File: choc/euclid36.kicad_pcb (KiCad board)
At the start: 2 copper layers, 248.2 x 127 mm, 112 parts, among them SW10 SW_PUSH, SW11 SW_PUSH, SW12 SW_PUSH, SW14 SW_PUSH, SW15 SW_PUSH, SW16 SW_PUSH, SW17 SW_PUSH, SW18 SW_PUSH, SW19 SW_PUSH, SW2 SW_PUSH, SW20 SW_PUSH, SW21 SW_PUSH, SW22 SW_PUSH, SW23 SW_PUSH, SW25 SW_PUSH, SW26 SW_PUSH, SW27 SW_PUSH, SW28 SW_PUSH, SW29 SW_PUSH, SW3 SW_PUSH, SW31 SW_PUSH, SW32 SW_PUSH, SW33 SW_PUSH, SW34 SW_PUSH, SW35 SW_PUSH, SW37 SW_PUSH, SW38 SW_PUSH, SW39 SW_PUSH, SW4 SW_PUSH, SW40 SW_PUSH, SW41 SW_PUSH, SW42 SW_PUSH, SW5 SW_PUSH, SW6 SW_PUSH, SW8 SW_PUSH, SW9 SW_PUSH, U2 ATmega32U4-MU, Y1 XTAL

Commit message: Wired everything. Not too happy with it, but I think it works
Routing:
- net VCC: track 0.00 -> 656.2 mm, vias 0 -> 30
- net col3: track 0.00 -> 541.0 mm, vias 0 -> 18
- net GND: track 164.3 -> 669.2 mm, vias 2 -> 12
- net col4: track 0.00 -> 501.9 mm, vias 0 -> 22
- net col2: track 0.00 -> 416.9 mm, vias 0 -> 17
- net col1: track 0.00 -> 387.6 mm, vias 0 -> 15
- net row6: track 0.00 -> 274.4 mm, vias 0 -> 6
- net col0: track 0.00 -> 231.2 mm, vias 0 -> 2
- net row5: track 0.00 -> 200.6 mm, vias 0 -> 4
- net col5: track 0.00 -> 193.8 mm, vias 0 -> 12
- net row3: track 0.00 -> 185.9 mm, vias 0 -> 10
- net row4: track 0.00 -> 169.3 mm, vias 0 -> 6
- net row2: track 0.00 -> 163.8 mm
- net row1: track 0.00 -> 137.2 mm
- net row0: track 9.49 -> 117.2 mm
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
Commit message: Small fixes
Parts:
- moved L6 1.40 mm to (47.3, 71.6)
- moved L11 1.17 mm to (252.7, 71.1)
- moved L5 0.85 mm to (64.0, 45.0)
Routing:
- net GND: track 669.2 -> 672.9 mm
- net Net-(L5-Pad2): track 69.8 -> 72.9 mm
- net Net-(L11-Pad2): track 27.8 -> 29.1 mm
- net Net-(L10-Pad2): track 45.2 -> 44.3 mm
- net VCC: track 656.2 -> 657.1 mm
- net Net-(L6-Pad2): track 80.9 -> 80.3 mm

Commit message: complete, ready for fabrication, though might change mini usb to micro usb before doing so
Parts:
- removed D1: PRTR5V0U2X, euclid36-libs:SOT-143B
- removed R3: 5.1k, Resistor_SMD:R_0805_2012Metric_Pad1.20x1.40mm_HandSolder
- added L14: WS2812B, euclid36-libs:SK6812-MINI-E, B.Cu at (122.2, 70.2)
- added L15: WS2812B, euclid36-libs:SK6812-MINI-E, B.Cu at (117.2, 88.6)
- added L16: WS2812B, euclid36-libs:SK6812-MINI-E, B.Cu at (91.3, 111.9)
- added L17: WS2812B, euclid36-libs:SK6812-MINI-E, B.Cu at (112.5, 120.2)
- added L18: WS2812B, euclid36-libs:SK6812-MINI-E, B.Cu at (131.9, 131.4)
- added L19: WS2812B, euclid36-libs:SK6812-MINI-E, B.Cu at (169.3, 131.4)
- added L20: WS2812B, euclid36-libs:SK6812-MINI-E, B.Cu at (188.7, 120.2)
- added L21: WS2812B, euclid36-libs:SK6812-MINI-E, B.Cu at (210.0, 111.9)
- added L22: WS2812B, euclid36-libs:SK6812-MINI-E, B.Cu at (184.0, 88.6)
- added L23: WS2812B, euclid36-libs:SK6812-MINI-E, B.Cu at (179.1, 70.2)
- added L24: WS2812B, euclid36-libs:SK6812-MINI-E, B.Cu at (174.1, 51.8)
- added L25: WS2812B, euclid36-libs:SK6812-MINI-E, B.Cu at (191.9, 44.4)
- added L26: WS2812B, euclid36-libs:SK6812-MINI-E, B.Cu at (196.8, 62.8)
- added L27: WS2812B, euclid36-libs:SK6812-MINI-E, B.Cu at (201.7, 81.2)
- added L28: WS2812B, euclid36-libs:SK6812-MINI-E, B.Cu at (218.8, 71.4)
- added L29: WS2812B, euclid36-libs:SK6812-MINI-E, B.Cu at (213.9, 53.0)
- added L30: WS2812B, euclid36-libs:SK6812-MINI-E, B.Cu at (209.0, 34.6)
- added L31: WS2812B, euclid36-libs:SK6812-MINI-E, B.Cu at (228.7, 34.6)
- added L32: WS2812B, euclid36-libs:SK6812-MINI-E, B.Cu at (233.6, 53.0)
- added L33: WS2812B, euclid36-libs:SK6812-MINI-E, B.Cu at (238.5, 71.4)
- added L34: WS2812B, euclid36-libs:SK6812-MINI-E, B.Cu at (259.6, 76.2)
- added L35: WS2812B, euclid36-libs:SK6812-MINI-E, B.Cu at (254.6, 57.8)
- added L36: WS2812B, euclid36-libs:SK6812-MINI-E, B.Cu at (249.7, 39.4)
- added R2: 10k, Resistor_SMD:R_0805_2012Metric, B.Cu at (141.0, 64.0)
- C1: value 1u -> 1uF
- C2, C3, C4: value 0.1u -> 0.1uF
- C7, C8: value 22p -> 22pF
- F1: value Polyfuse_Small -> 500mA; footprint Fuse:Fuse_1206_3216Metric_Pad1.42x1.75mm_HandSolder -> Fuse:Fuse_1206_3216Metric
- L1, L2, L3: footprint LED_SMD:LED_WS2812B_PLCC4_5.0x5.0mm_P3.2mm -> euclid36-libs:SK6812-MINI-E; moved to B.Cu
- L10, L11, L12, L13, L4, L5, L6, L7, L8, L9: footprint LED_SMD:LED_WS2812B_PLCC4_5.0x5.0mm_P3.2mm -> euclid36-libs:SK6812-MINI-E
- R1: footprint Resistor_SMD:R_0805_2012Metric_Pad1.20x1.40mm_HandSolder -> Resistor_SMD:R_0805_2012Metric
- R4, R5: value R_Small -> 22; footprint Resistor_SMD:R_0805_2012Metric_Pad1.20x1.40mm_HandSolder -> Resistor_SMD:R_0805_2012Metric
- SW10, SW11, SW12, SW14, SW15, SW16, SW17, SW18, SW19, SW2, SW20, SW21, SW22, SW23, SW25, SW26, SW27, SW28, SW29, SW3, SW31, SW32, SW33, SW34, SW35, SW37, SW38, SW39, SW4, SW40, SW41, SW42, SW5, SW6, SW8, SW9: footprint euclid36-libs:KailhChoc-1U -> euclid36-libs:Kailh_socket_PG1350
- U2: value ATmega32U4-MU -> ATmega32U4-AU; footprint Package_DFN_QFN:QFN-44-1EP_7x7mm_P0.5mm_EP5.2x5.2mm -> Package_QFP:TQFP-44_10x10mm_P0.8mm
- USB1: value HRO-TYPE-C-31-M-12 -> Molex-0548190589; footprint euclid36-libs:HRO-TYPE-C-31-M-12-HandSoldering -> euclid36-libs:Molex-0548190589
- Y1: footprint Crystal:Crystal_SMD_3225-4Pin_3.2x2.5mm_HandSoldering -> Crystal:Crystal_SMD_3225-4Pin_3.2x2.5mm
- moved L11 148.5 mm to (104.4, 62.8), turned to 165 degrees
- moved L10 136.3 mm to (99.5, 81.2), turned to 165 degrees
- moved L12 127.7 mm to (109.3, 44.4), turned to 165 degrees
- moved L3 125.0 mm to (41.7, 76.2), turned to 345 degrees
- moved L9 106.3 mm to (82.4, 71.4), turned to 345 degrees
- moved L1 104.4 mm to (51.5, 39.4), turned to 345 degrees
- moved L2 97.0 mm to (46.6, 57.8), turned to 345 degrees
- moved L8 79.3 mm to (87.3, 53.0), turned to 345 degrees
- moved L7 76.5 mm to (92.3, 34.6), turned to 345 degrees
- moved L13 60.8 mm to (127.1, 51.8), turned to 345 degrees
- moved L4 54.6 mm to (62.7, 71.4), turned to 165 degrees
- moved L6 44.8 mm to (72.5, 34.6), turned to 165 degrees
- moved SW42 43.6 mm to (211.2, 116.0), turned to 15 degrees
- moved Y1 41.9 mm to (151.6, 64.5), turned to 180 degrees
- moved C8 41.0 mm to (147.1, 64.5), turned to 270 degrees
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- renumbered C6 to C5, REF** to H1, REF** to H2, REF** to H3, REF** to H4, REF** to H5, REF** to H6, REF** to H7, REF** to H8
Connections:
- R4 pad 2: Net-(D1-Pad3) -> Net-(R4-Pad2)
- R5 pad 2: Net-(D1-Pad2) -> Net-(R5-Pad2)
- U2 pad 1: row0 -> Net-(U2-Pad1)
- U2 pad 10: Net-(U2-Pad10) -> row0
- U2 pad 18: col5 -> Net-(U2-Pad18)
- U2 pad 25: Net-(U2-Pad25) -> row3
- U2 pad 26: Net-(U2-Pad26) -> row4
- U2 pad 27: Net-(U2-Pad27) -> row5
- U2 pad 28: col0 -> Net-(U2-Pad28)
- U2 pad 29: col1 -> Net-(U2-Pad29)
- U2 pad 30: col2 -> Net-(U2-Pad30)
- U2 pad 31: col3 -> Net-(U2-Pad31)
- U2 pad 32: col4 -> row6
- U2 pad 36: row6 -> col0
- U2 pad 37: row5 -> col1
- U2 pad 38: row4 -> col2
- U2 pad 39: row3 -> col3
- U2 pad 40: row2 -> col4
- U2 pad 41: row1 -> col5
- U2 pad 7: Net-(U2-Pad7) -> +5V
- U2 pad 8: Net-(U2-Pad8) -> row2
- U2 pad 9: LED -> row1
- USB1 pad 1: GND -> +5V
- USB1 pad 2: VCC -> Net-(USB1-Pad2)
- USB1 pad 3: Net-(USB1-Pad3) -> Net-(R5-Pad2)
- USB1 pad 4: Net-(R3-Pad1) -> Net-(R4-Pad2)
- USB1 pad 5: Net-(D1-Pad3) -> VCC
- USB1 pad 6: Net-(D1-Pad2) -> Net-(USB1-Pad6)
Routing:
- net GND: track 672.9 -> 1411.3 mm, vias 12 -> 50
- net VCC: track 657.1 -> 1222.7 mm, vias 30 -> 47
- net col3: track 541.0 -> 388.4 mm, vias 18 -> 11
- net +5V: track 34.5 -> 161.2 mm, vias 2 -> 9
- net Net-(L21-Pad2): track 0.00 -> 90.2 mm, vias 0 -> 6
- net col4: track 501.9 -> 415.4 mm, vias 22 -> 7
- net row5: track 200.6 -> 124.0 mm, vias 4 -> 0
- net col5: track 193.8 -> 258.2 mm, vias 12 -> 7
- net Net-(L7-Pad2): track 82.8 -> 21.3 mm
- net Net-(L3-Pad2): track 91.7 -> 31.6 mm, vias 3 -> 2
- net Net-(L18-Pad2): track 0.00 -> 58.5 mm
- net Net-(L10-Pad4): track 84.3 -> 27.3 mm
- net Net-(L6-Pad2): track 80.3 -> 24.4 mm
- net row3: track 185.9 -> 130.7 mm, vias 10 -> 0
- net row4: track 169.3 -> 114.6 mm, vias 6 -> 0
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
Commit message: Updated choc version to use usb-c. Almost done, still need to create a case / svgs
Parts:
- removed F1: 500mA, Fuse:Fuse_1206_3216Metric
- added C6: 4.7n, Capacitor_SMD:C_0805_2012Metric, B.Cu at (143.5, 30.0)
- added C9: 4.7n, Capacitor_SMD:C_0805_2012Metric, B.Cu at (145.8, 36.1)
- added R3: 1M, Resistor_SMD:R_0805_2012Metric, B.Cu at (158.8, 29.7)
- added R6: 5.1k, Resistor_SMD:R_0805_2012Metric, B.Cu at (149.9, 37.3)
- added R7: 5.1k, Resistor_SMD:R_0805_2012Metric, B.Cu at (155.2, 37.3)
- added R8: 1.5K, Resistor_SMD:R_0805_2012Metric, B.Cu at (152.4, 37.3)
- added U1: USBLC6-2SC6, Package_TO_SOT_SMD:SOT-23-6, B.Cu at (159.0, 37.6)
- R4, R5: value 22 -> 22R
- USB1: value Molex-0548190589 -> HRO-TYPE-C-31-M-12; footprint euclid36-libs:Molex-0548190589 -> euclid36-libs:HRO-TYPE-C-31-M-12-Assembly
- moved R2 14.4 mm to (141.5, 44.9)
- moved R5 8.29 mm to (160.3, 42.7)
- moved R4 7.85 mm to (157.2, 42.7)
- moved USB1 3.84 mm to (151.1, 25.4), turned to 0 degrees
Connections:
- USB1 pad 1: +5V -> GND
- USB1 pad 2: Net-(USB1-Pad2) -> VBUS
- USB1 pad 3: Net-(R5-Pad2) -> Net-(USB1-Pad3)
- USB1 pad 4: Net-(R4-Pad2) -> Net-(R6-Pad2)
- USB1 pad 5: VCC -> D-BUS
- USB1 pad 6: Net-(USB1-Pad6) -> D+BUS
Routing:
- net +5V: track 161.2 -> 89.8 mm, vias 9 -> 6
- net GND: track 1411.3 -> 1445.9 mm, vias 50 -> 48
- net VBUS: track 0.00 -> 28.9 mm, vias 0 -> 3
- net VCC: track 1222.7 -> 1195.3 mm
- net D+BUS: track 0.00 -> 22.0 mm, vias 0 -> 2
- net Net-(C6-Pad1): track 0.00 -> 21.3 mm
- net Net-(R7-Pad2): track 0.00 -> 20.4 mm, vias 0 -> 2
- net Net-(USB1-Pad6): track 19.8 -> 0.00 mm, vias 2 -> 0
- net D-BUS: track 0.00 -> 18.9 mm, vias 0 -> 4
- net D+: track 45.2 -> 50.9 mm
- net D-: track 47.7 -> 52.5 mm
- net Net-(R6-Pad2): track 0.00 -> 3.34 mm
- net Net-(R5-Pad2): track 4.77 -> 3.20 mm
- net Net-(R4-Pad2): track 4.43 -> 3.41 mm

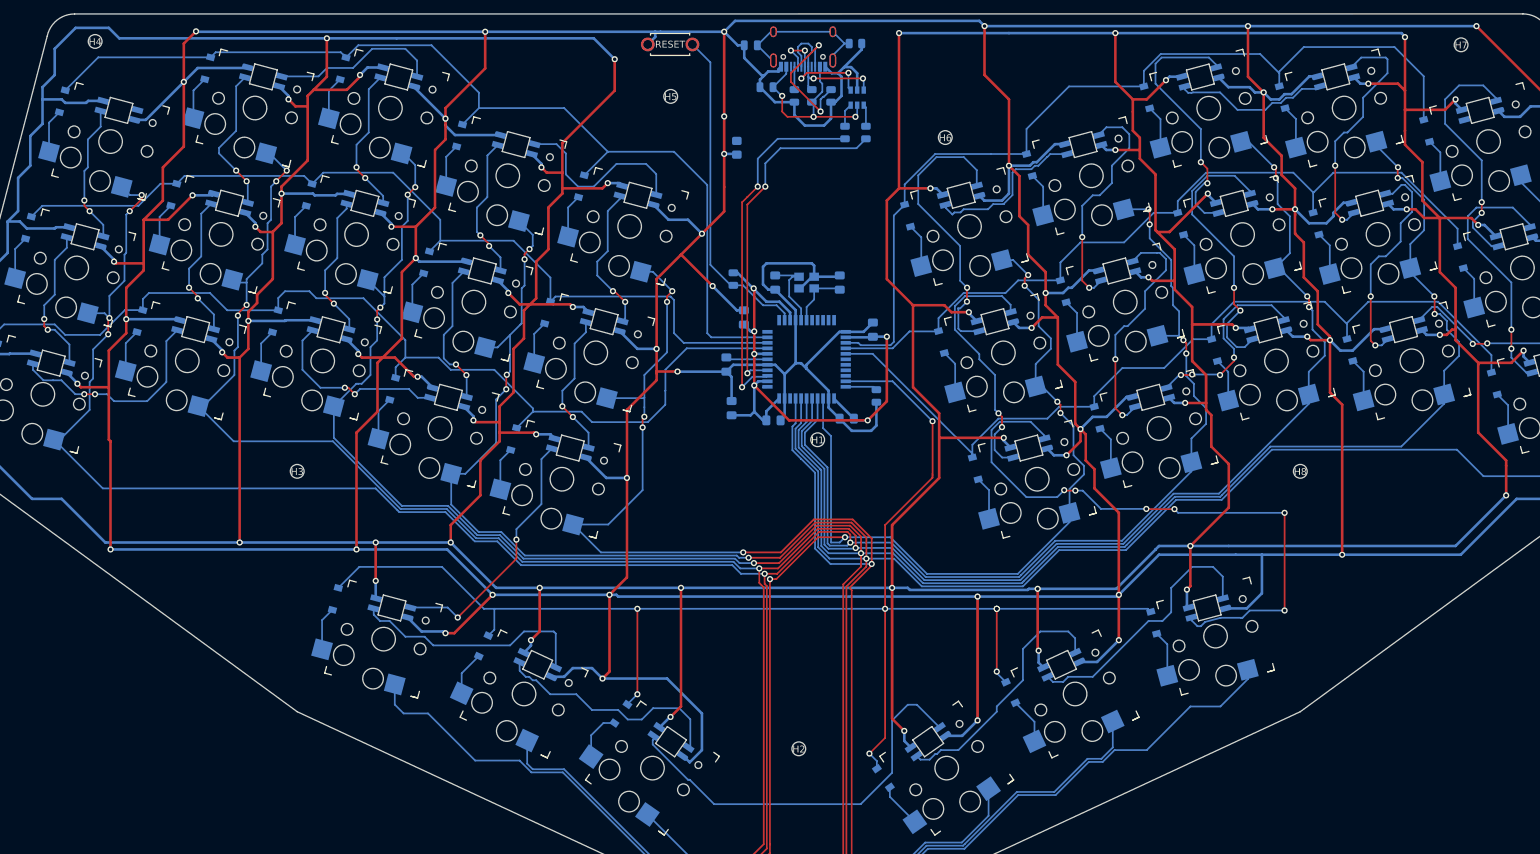
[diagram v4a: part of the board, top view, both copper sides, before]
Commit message: Updated to include mounting holes and gerber update
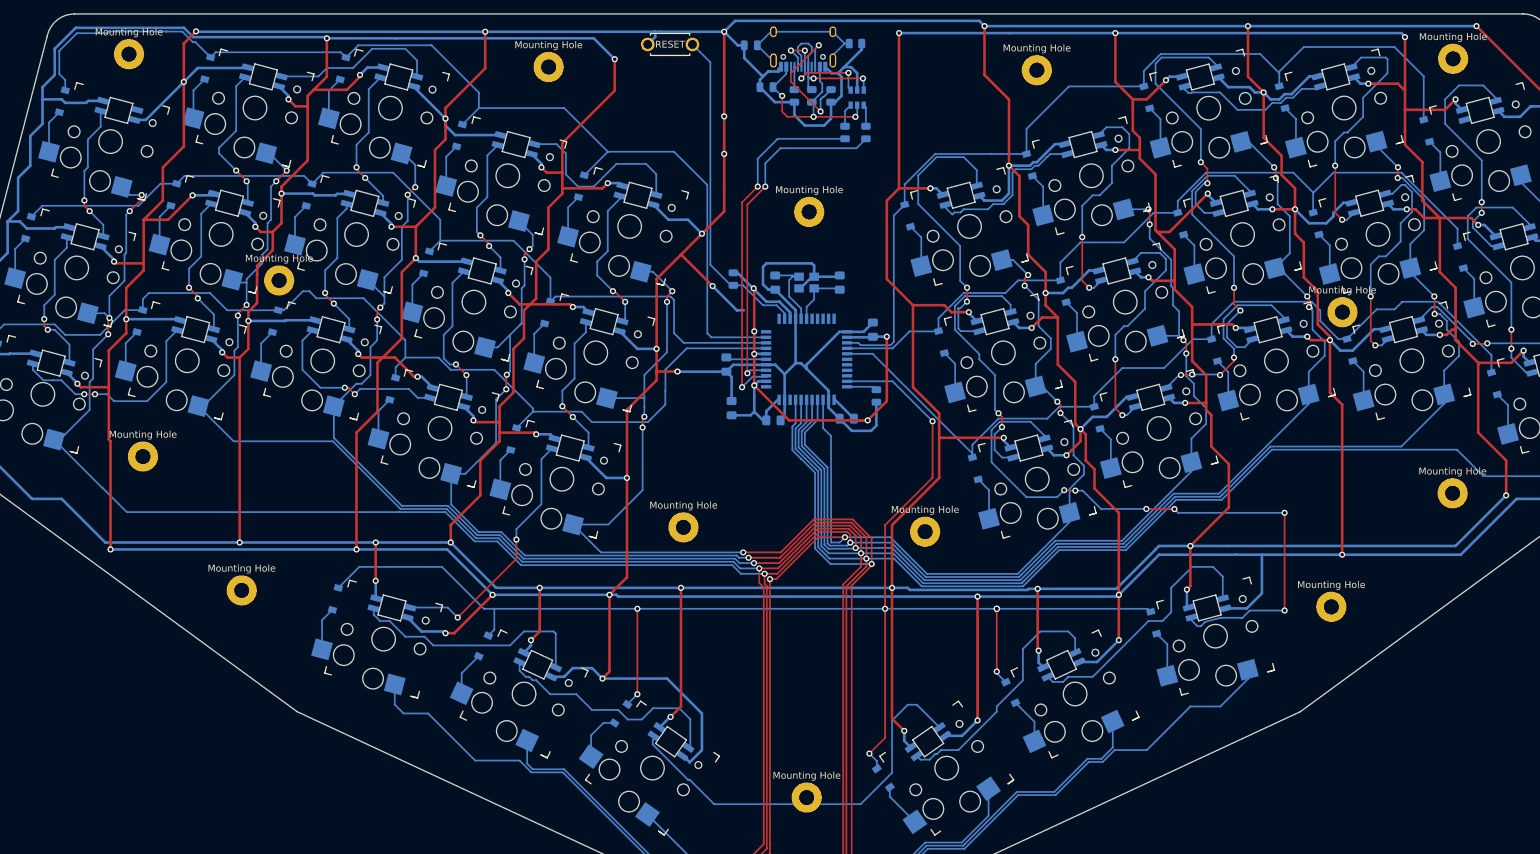
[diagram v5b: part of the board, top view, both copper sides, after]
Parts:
- removed the C5 at (142.5, 69.6)
- removed H1, H2, H3, H4, H5, H6, H7, H8: M2_Hole_NPTH_Outside, _reviung-kbd:M2_Hole_NPTH_Outside
- removed the R2 at (141.5, 44.9)
- added Mounting Hole: MountingHole_2.2mm_M2_Pad, MountingHole:MountingHole_2.2mm_M2_Pad, F.Cu at (229.7, 68.8)
- added Mounting Hole: MountingHole_2.2mm_M2_Pad, MountingHole:MountingHole_2.2mm_M2_Pad, F.Cu at (53.0, 31.3)
- added Mounting Hole: MountingHole_2.2mm_M2_Pad, MountingHole:MountingHole_2.2mm_M2_Pad, F.Cu at (245.8, 31.9)
- added Mounting Hole: MountingHole_2.2mm_M2_Pad, MountingHole:MountingHole_2.2mm_M2_Pad, F.Cu at (114.1, 33.1)
- added Mounting Hole: MountingHole_2.2mm_M2_Pad, MountingHole:MountingHole_2.2mm_M2_Pad, F.Cu at (185.2, 33.6)
- added Mounting Hole: MountingHole_2.2mm_M2_Pad, MountingHole:MountingHole_2.2mm_M2_Pad, F.Cu at (152.0, 54.2)
- added Mounting Hole: MountingHole_2.2mm_M2_Pad, MountingHole:MountingHole_2.2mm_M2_Pad, F.Cu at (74.8, 64.2)
- added Mounting Hole: MountingHole_2.2mm_M2_Pad, MountingHole:MountingHole_2.2mm_M2_Pad, F.Cu at (228.0, 111.7)
- added Mounting Hole: MountingHole_2.2mm_M2_Pad, MountingHole:MountingHole_2.2mm_M2_Pad, F.Cu at (55.0, 89.8)
- added Mounting Hole: MountingHole_2.2mm_M2_Pad, MountingHole:MountingHole_2.2mm_M2_Pad, F.Cu at (245.7, 95.2)
- added Mounting Hole: MountingHole_2.2mm_M2_Pad, MountingHole:MountingHole_2.2mm_M2_Pad, F.Cu at (168.9, 100.8)
- added Mounting Hole: MountingHole_2.2mm_M2_Pad, MountingHole:MountingHole_2.2mm_M2_Pad, F.Cu at (133.7, 100.2)
- added Mounting Hole: MountingHole_2.2mm_M2_Pad, MountingHole:MountingHole_2.2mm_M2_Pad, F.Cu at (151.7, 139.5)
- added Mounting Hole: MountingHole_2.2mm_M2_Pad, MountingHole:MountingHole_2.2mm_M2_Pad, F.Cu at (69.4, 109.3)
- U2: footprint Package_QFP:TQFP-44_10x10mm_P0.8mm -> euclid36-libs:ATMEGA32U4-AU
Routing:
- net row0: track 145.4 -> 153.1 mm
- net +5V: track 89.8 -> 87.9 mm
- net GND: track 1445.9 -> 1444.1 mm
- net row2: track 145.6 -> 144.5 mm

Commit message: latest low pro choc keyboard
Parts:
- removed Mounting Hole: MountingHole_2.2mm_M2_Pad, MountingHole:MountingHole_2.2mm_M2_Pad (x14)
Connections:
- U2 pad 11: Net-(U2-Pad11) -> LED
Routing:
- net LED: track 0.00 -> 144.2 mm, vias 0 -> 6
- net GND: track 1444.1 -> 1431.6 mm, vias 48 -> 47
